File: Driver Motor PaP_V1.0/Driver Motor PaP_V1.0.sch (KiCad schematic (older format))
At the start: 27 parts, among them J1 Conn_01x02, J2 Conn_01x02, J3 Conn_01x02, J4 Conn_01x04, J5 Conn_01x01, J6 Conn_01x02, J7 Conn_01x02, U1 LM358, U2 LM358, U3 LM358

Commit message: Corrección que sugirio el revisador
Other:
- note added: "Alimentación de los amplificadores \noperacionales - LM358"
- note added: "Conector - sentido de giro del eje del motor.\nConector - tren de pulso."
- note removed: "Conector - sentido de giro.\nConector - tren de pulso."
- moved on the sheet: D1, J1, J2, R1, U1C, U2C, U3C

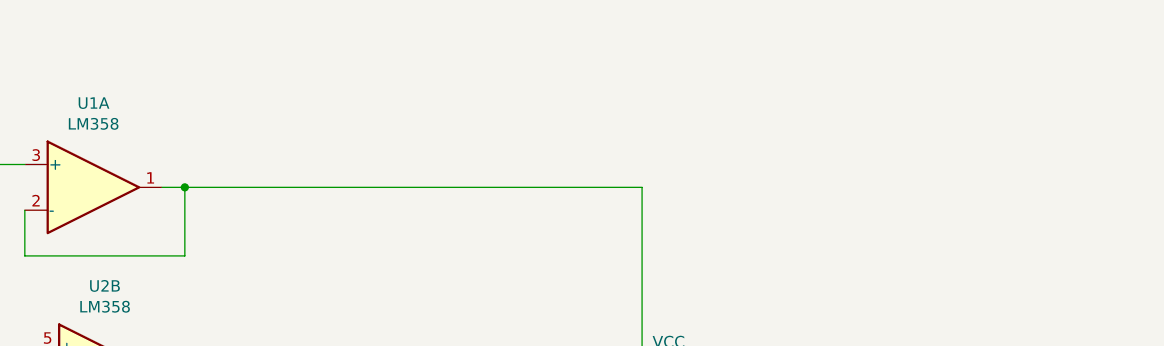
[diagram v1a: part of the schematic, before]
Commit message: Corrección de las sugerencia del revisor 1.1
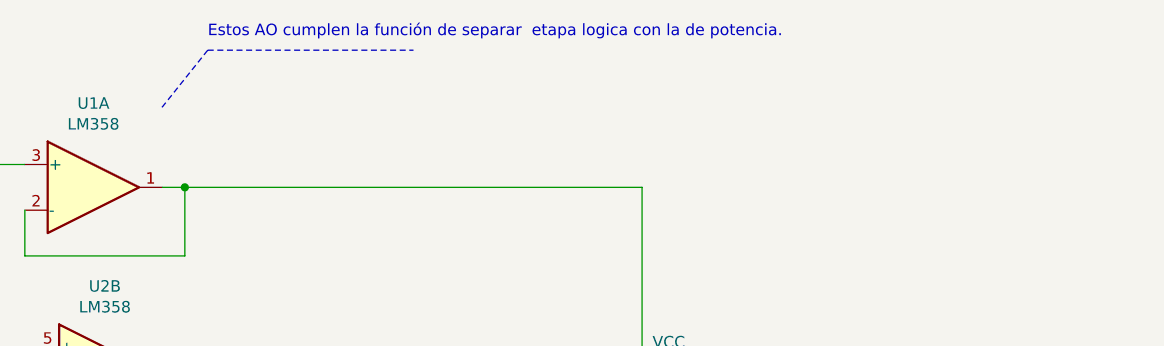
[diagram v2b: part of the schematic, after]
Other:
- note added: "Estos AO cumplen la función de separar etapa logica con la de potencia.\n"
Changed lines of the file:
@@
 Text Notes 2500 5650 0    50   ~ 0
 Alimentación de los amplificadores \noperacionales - LM358
+Wire Notes Line
+	5700 1050 5900 800
+Wire Notes Line
+	5900 800  6800 800
+Text Notes 5900 750  0    50   ~ 0
+Estos AO cumplen la función de separar  etapa logica con la de potencia.\n
 $EndSCHEMATC

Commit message: PCB Driver Motor PaP
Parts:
- removed J3: Conn_01x02, Connector_PinHeader_2.54mm:PinHeader_1x02_P2.54mm_Vertical, symbol Connector_Generic:Conn_01x02
- removed J4: Conn_01x04, Connector_PinHeader_2.54mm:PinHeader_1x04_P2.54mm_Vertical, symbol Connector_Generic:Conn_01x04
- added C2, C3, C4: 100nF, Capacitor_SMD:C_0805_2012Metric_Pad1.15x1.40mm_HandSolder, symbol Device:C
- added FID1: Fiducial, Fiducial:Fiducial_1mm_Mask2mm, symbol Mechanical:Fiducial
- added J3: Conn_01x03, Connector_Molex:Molex_KK-254_AE-6410-03A_1x03_P2.54mm_Vertical, symbol Connector_Generic:Conn_01x03
- added J4: Conn_01x05, Connector_Molex:Molex_KK-254_AE-6410-05A_1x05_P2.54mm_Vertical, symbol Connector_Generic:Conn_01x05
- C1: footprint Capacitor_THT:C_Radial_D6.3mm_H11.0mm_P2.50mm -> Capacitor_SMD:CP_Elec_6.3x5.4
- D1: footprint LED_THT:LED_D3.0mm -> LED_SMD:LED_0805_2012Metric_Pad1.15x1.40mm_HandSolder
- H1, H2, H3, H4: footprint MountingHole:MountingHole_3mm_Pad -> MountingHole:MountingHole_3.2mm_M3
- J1, J2: footprint Connector_PinHeader_2.54mm:PinHeader_1x02_P2.54mm_Vertical -> TerminalBlock:TerminalBlock_bornier-2_P5.08mm
- R1: footprint Resistor_THT:R_Axial_DIN0207_L6.3mm_D2.5mm_P10.16mm_Horizontal -> Resistor_SMD:R_0805_2012Metric_Pad1.15x1.40mm_HandSolder
- U1, U2, U3: footprint Package_DIP:DIP-8_W7.62mm -> Package_SO:SOIC-8_3.9x4.9mm_P1.27mm
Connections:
- net GND: now also C2.2, C3.2, C4.2, J3.3 (Pin_3), J4.5 (Pin_5)
- net VCC: now also C2.1, C3.1, C4.1
- net at U2.3 (+): now also J4.1 (Pin_1)
- net at U1.5 (+): now also J3.2 (Pin_2)
- net at U3.3 (+): now also J4.3 (Pin_3)
- net at U3.5 (+): now also J4.4 (Pin_4)
- net at U1.3 (+): now also J3.1 (Pin_1)
- net at U2.5 (+): now also J4.2 (Pin_2)
- net at U2.6 (-), U2.7: now also JP5.1 (A); no longer A1.16 (DIR)
- net at U1.6 (-), U1.7: now also A1.16 (DIR); no longer JP5.1 (A)
- net GNDMotor renamed GNDPWR
- net VMotor renamed VPP
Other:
- note added: "Pin 1 - recibe tren de pulso .\nPin 2 - establece sentido de giro del eje del motor."
- note added: "este conector permite hacer uso del amplificador \npara fururo en caso de ser necesario."
- note removed: "Conector - sentido de giro del eje del motor.\nConector - tren de pulso."
- moved on the sheet: C1, D1, H4, J1, J2, R1, U1B, U1C, U2B, U2C, U3C

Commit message: correcciones driver motor PaP v1.0
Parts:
- A1: N° Catalogo (none) -> 2133 - Pololu Robotics Electronics
- U1: Código Catalogo (none) -> 511-LM358D
- U2, U3: N° Catalogo (none) -> 511-LM358D
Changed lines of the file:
@@
 F 2 "Module:Pololu_Breakout-16_15.2x20.3mm" H 8700 2300 50  0001 L CNN
 F 3 "https://www.pololu.com/product/2982" H 8600 2800 50  0001 C CNN
+F 4 "2133 - Pololu Robotics Electronics" H 8500 3100 50  0001 C CNN "N° Catalogo"
 	1    8500 3100
 	1    0    0    -1
@@
 F 2 "Package_SO:SOIC-8_3.9x4.9mm_P1.27mm" H 5400 1400 50  0001 C CNN
 F 3 "http://www.ti.com/lit/ds/symlink/lm2904-n.pdf" H 5400 1400 50  0001 C CNN
+F 4 "511-LM358D" H 5400 1400 50  0001 C CNN "Código Catalogo"
 	1    5400 1400
 	1    0    0    -1
@@
 F 2 "Package_SO:SOIC-8_3.9x4.9mm_P1.27mm" H 5400 3950 50  0001 C CNN
 F 3 "http://www.ti.com/lit/ds/symlink/lm2904-n.pdf" H 5400 3950 50  0001 C CNN
+F 4 "511-LM358D" H 5400 3950 50  0001 C CNN "N° Catalogo"
 	2    5400 3950
 	1    0    0    -1
@@
 F 2 "Package_SO:SOIC-8_3.9x4.9mm_P1.27mm" H 5450 5850 50  0001 C CNN
 F 3 "http://www.ti.com/lit/ds/symlink/lm2904-n.pdf" H 5450 5850 50  0001 C CNN
+F 4 "511-LM358D" H 5450 5850 50  0001 C CNN "N° Catalogo"
 	2    5450 5850
 	1    0    0    -1

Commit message: Agregado:fabricante, pieza y biblioteca de footprint y componentes
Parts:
- A1: Fabricante (none) -> Pololu Corporation; N° Catalogo 2133 - Pololu Robotics Electronics -> (none); N° de Pieza del Fabricante (none) -> 2133; digi-key # (none) -> 2183-2133-ND
- C1: Fabricante (none) -> Nichicon; N° de Pieza del Fabricante (none) -> UWT1H101MNL1GS; digi-key # (none) -> 493-226-1-ND
- C2, C3, C4: Fabricante (none) -> Murata Electronics; N° de Pieza del Fabricante (none) -> GRM31CD80J107ME39K; digi-key # (none) -> 490-16313-2-ND
- J1, J2: Fabricante (none) -> TE Connectivity AMP Connectors; N° de Pieza del Fabricante (none) -> 282837-2; digi-key # (none) -> A113320-ND
- J3: Fabricante (none) -> Molex; N° de Pieza del Fabricante (none) -> 0022272031; digi-key # (none) -> WM411-ND
- J4: Fabricante (none) -> Molex; N° de Pieza del Fabricante (none) -> 0022272051; digi-key # (none) -> WM4114-ND
- J5: Fabricante (none) -> Molex; N° de Pieza del Fabricante (none) -> 0022284010; digi-key # (none) -> WM50014-01-ND
- J6, J7, JP1, JP2, JP3, JP4, JP5, JP6, JP7, JP8, JP9: Fabricante (none) -> Molex; N° de Pieza del Fabricante (none) -> 0901200122; digi-key # (none) -> WM8072-ND
- U1, U2, U3: Fabricante (none) -> STMicroelectronics; N° de Pieza del Fabricante (none) -> LM358DT; digi-key # (none) -> 497-1591-2-ND
- U2, U3: Fabricante (none) -> STMicroelectronics; N° Catalogo 511-LM358D -> (none); N° de Pieza del Fabricante (none) -> LM358DT; digi-key # (none) -> 497-1591-2-ND

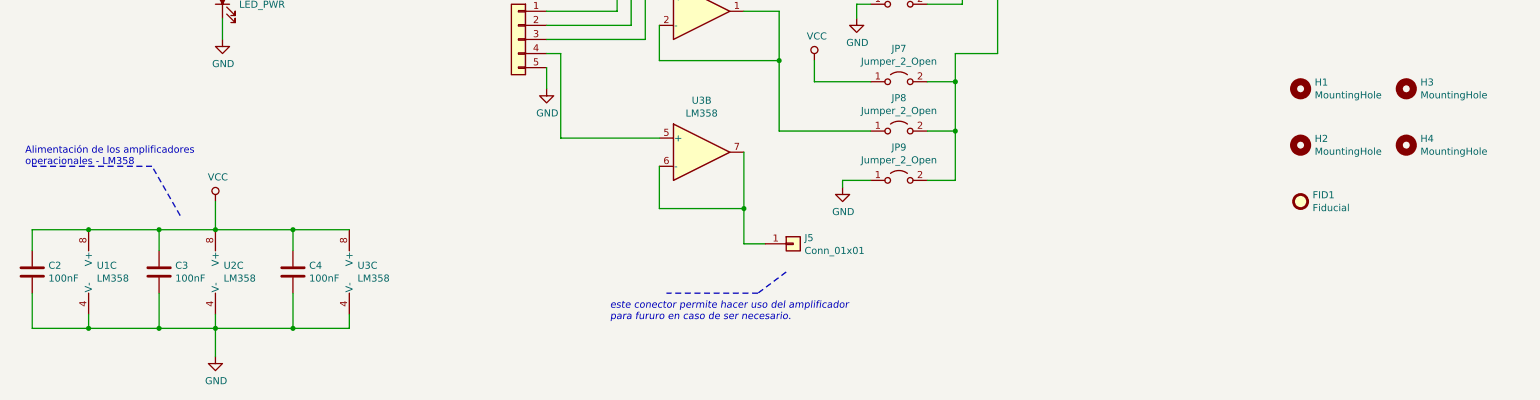
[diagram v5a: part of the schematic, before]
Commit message: modificación de margen y traslado de componentes a la capa superior
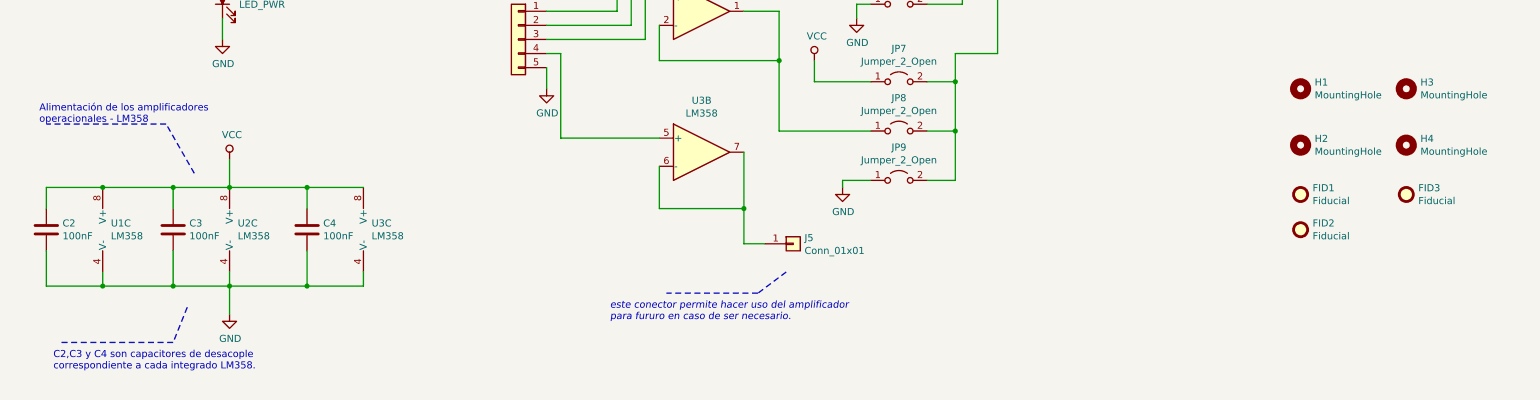
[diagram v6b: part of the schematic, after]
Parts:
- added FID2, FID3: Fiducial, Fiducial:Fiducial_1mm_Mask2mm, symbol Mechanical:Fiducial
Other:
- note added: "C2,C3 y C4 son capacitores de desacople \ncorrespondiente a cada integrado LM358."
- moved on the sheet: C2, C3, C4, FID1, U1C, U2C, U3C

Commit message: correción dehuellas delos terminales block y modelo 3D
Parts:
- J1, J2: footprint TerminalBlock:TerminalBlock_bornier-2_P5.08mm -> TerminalBlock_Phoenix:TerminalBlock_Phoenix_MKDS-1,5-2-5.08_1x02_P5.08mm_Horizontal
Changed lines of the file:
@@
 F 0 "J2" H 1268 1517 50  0000 C CNN
 F 1 "Conn_01x02" H 1268 1426 50  0000 C CNN
-F 2 "TerminalBlock:TerminalBlock_bornier-2_P5.08mm" H 1350 1300 50  0001 C CNN
+F 2 "TerminalBlock_Phoenix:TerminalBlock_Phoenix_MKDS-1,5-2-5.08_1x02_P5.08mm_Horizontal" H 1350 1300 50  0001 C CNN
 F 3 "https://www.te.com/commerce/DocumentDelivery/DDEController?Action=srchrtrv&DocNm=282837&DocType=Customer+Drawing&DocLang=English" H 1350 1300 50  0001 C CNN
 F 4 "	TE Connectivity AMP Connectors" H 1350 1300 50  0001 C CNN "Fabricante"
@@
 F 0 "J1" H 1618 3217 50  0000 C CNN
 F 1 "Conn_01x02" H 1618 3126 50  0000 C CNN
-F 2 "TerminalBlock:TerminalBlock_bornier-2_P5.08mm" H 1700 3000 50  0001 C CNN
+F 2 "TerminalBlock_Phoenix:TerminalBlock_Phoenix_MKDS-1,5-2-5.08_1x02_P5.08mm_Horizontal" H 1700 3000 50  0001 C CNN
 F 3 "https://www.te.com/commerce/DocumentDelivery/DDEController?Action=srchrtrv&DocNm=282837&DocType=Customer+Drawing&DocLang=English" H 1700 3000 50  0001 C CNN
 F 4 "	TE Connectivity AMP Connectors" H 1700 3000 50  0001 C CNN "Fabricante"
